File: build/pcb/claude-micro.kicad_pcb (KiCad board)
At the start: 2 copper layers, 128 x 88 mm, 95 parts, among them SW1 Kailh Choc v1, SW10 Kailh Choc v1, SW11 Kailh Choc v1, SW12 Kailh Choc v1, SW13 Kailh Choc v1, SW2 Kailh Choc v1, SW3 Kailh Choc v1, SW4 Kailh Choc v1, SW5 Kailh Choc v1, SW6 Kailh Choc v1, SW7 Kailh Choc v1, SW8 Kailh Choc v1, SW9 Kailh Choc v1, U2 74LVC1G17

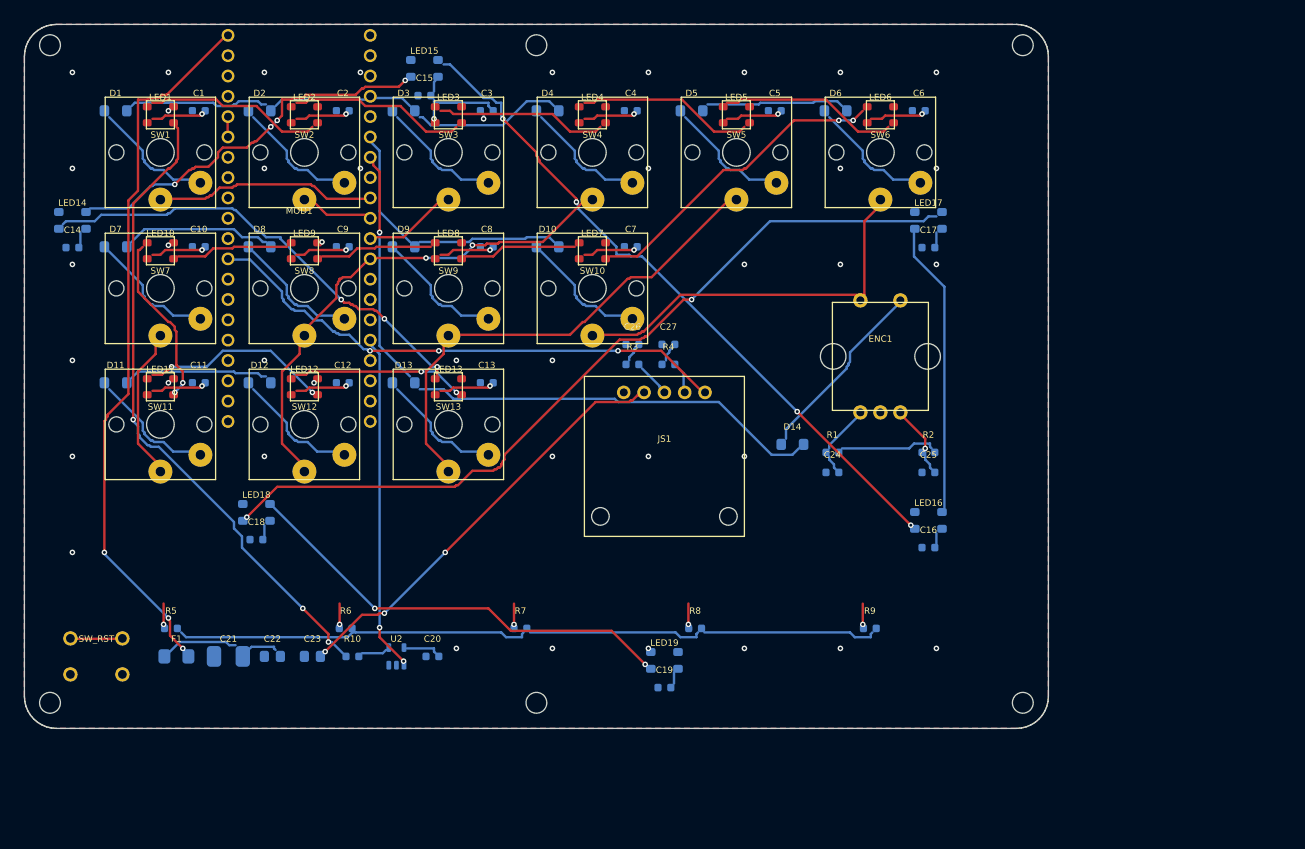
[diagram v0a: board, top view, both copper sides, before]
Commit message: Switch to clear MX switches; fix the EasyEDA project wrapper
Two changes.

EasyEDA
-------
The project wrapper now matches what EasyEDA 6.5 actually writes: docType is
the string "5" (not the integer 5), colors is an object, editorVersion sits at
the top level alongside a description, and each sheet carries its own string
docType and description. The 4.x shape I had reverse-engineered from an older
exported file would not round-trip. The structural test now asserts the exact
key set and types on both the project and the sheet.

Switches
--------
Kailh Choc low-profile replaced with clear-housing MX-compatible switches,
5-pin PCB mount. That is not a drop-in: MX needs a 19.05 mm grid where Choc
ran at 18 x 17, so the whole device re-derives from the config.

- footprint: two contacts at (-3.81, 2.54) and (2.54, 5.08), centre boss and
  two locating posts, 14 mm plate cutout, both contacts on the south half so
  the north half stays clear for the per-key LED in the switch's light window
- keycaps: 18 x 18 mm with a cross socket instead of Choc's twin posts, so
  bought MX caps drop in as an alternative to printing them
- Z stack rebuilt for 4 mm travel and an 11.6 mm body; the taller stack means
  the encoder now takes a stock 12.5 mm shaft rather than a trimmed one
- board 128 x 88 -> 159 x 102 mm, case 134 x 94 -> 165 x 108 mm, and the MCU
  module moved to the gutters of the new grid (pin columns at x=9.25 and
  x=27.03) so its through-holes still miss every top-side pad
- switches render translucent in the viewer to match the clear housings

The switch footprint name is now read from the config rather than hardcoded in
the ERC and two tests, which is what caught the 0-switches-for-13-keys error
after the swap.

Rebuilt and re-verified: 141/141 connections routed, 0 DRC errors, 0 warnings,
9/9 meshes watertight, 36/36 checks passing.

Co-Authored-By: Claude Opus 5 <noreply@anthropic.com>
Claude-Session: https://claude.ai/code/session_018r1gdNJN1A3uPDEU4991Ag
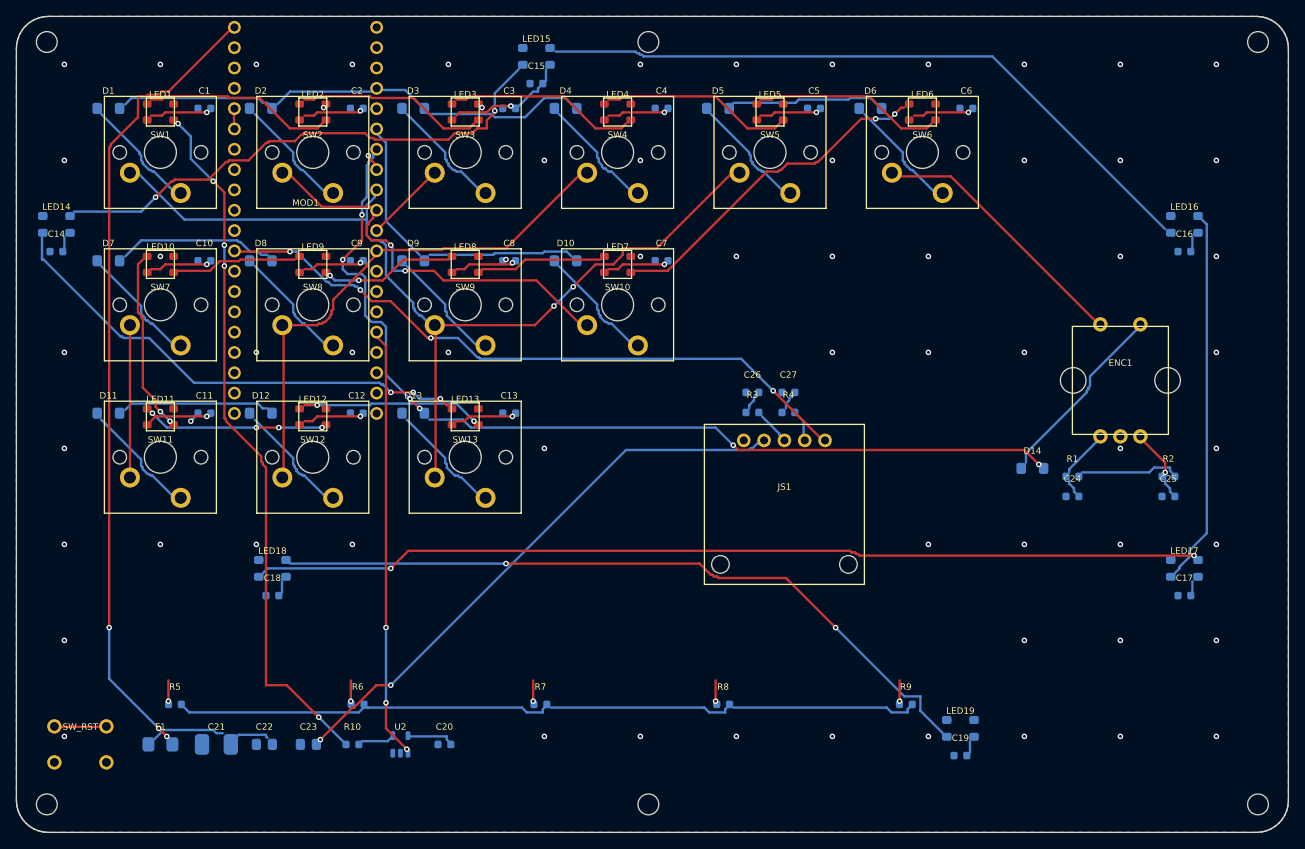
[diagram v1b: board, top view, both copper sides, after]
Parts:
- removed the ? at (-13.8, -13.4)
- removed the ? at (47.0, -13.4)
- removed the ? at (107.8, -13.4)
- removed the ? at (-13.8, 68.8)
- removed the ? at (47.0, 68.8)
- removed the ? at (107.8, 68.8)
- added ?: , claude-micro:MountingHole, F.Cu at (-14.2, -13.8)
- added ?: , claude-micro:MountingHole, F.Cu at (61.0, -13.8)
- added ?: , claude-micro:MountingHole, F.Cu at (137.2, -13.8)
- added ?: , claude-micro:MountingHole, F.Cu at (-14.2, 81.5)
- added ?: , claude-micro:MountingHole, F.Cu at (61.0, 81.5)
- added ?: , claude-micro:MountingHole, F.Cu at (137.2, 81.5)
- SW1, SW10, SW11, SW12, SW13, SW2, SW3, SW4, SW5, SW6, SW7, SW8, SW9: value Kailh Choc v1 -> MX clear; footprint claude-micro:Choc_v1 -> claude-micro:MX_PCB
- moved C17 54.0 mm to (128.0, 55.4)
- moved LED17 54.0 mm to (128.0, 52.0)
- moved C16 48.9 mm to (128.0, 12.4)
- moved LED16 48.9 mm to (128.0, 9.00)
- moved C19 38.0 mm to (100.0, 75.4)
- moved LED19 38.0 mm to (100.0, 72.0)
- moved C24 30.1 mm to (114.0, 43.0)
- moved C25 30.1 mm to (126.0, 43.0)
- moved D14 30.1 mm to (109.0, 39.5)
- moved ENC1 30.1 mm to (120.0, 28.5)
- moved R1 30.1 mm to (114.0, 40.5)
- moved R2 30.1 mm to (126.0, 40.5)
- moved C26 16.2 mm to (74.0, 30.0)
- moved C27 16.2 mm to (78.5, 30.0)
- moved JS1 16.2 mm to (78.0, 44.0)
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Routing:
- net ROW3: track 79.8 -> 117.6 mm, vias 1 -> 6
- net LED_D18: track 54.5 -> 91.4 mm
- net COL0: track 81.9 -> 111.3 mm, vias 0 -> 2
- net COL1: track 52.6 -> 78.8 mm, vias 0 -> 2
- net LED_D14: track 47.6 -> 65.6 mm, vias 4 -> 2
- net +3V3: track 65.6 -> 83.3 mm, vias 3 -> 2
- net JOY_SW: track 65.5 -> 82.0 mm, vias 3 -> 4
- net LED_D17: track 102.4 -> 117.8 mm
- net +5V: track 112.7 -> 127.0 mm
- net LED_DIN_3V3: track 41.1 -> 52.9 mm, vias 2 -> 3
- net VBUS: track 88.1 -> 99.3 mm
- net LED_D16: track 36.0 -> 46.1 mm
- net LED_DIN: track 80.1 -> 87.3 mm, vias 3 -> 5
- net ROW2: track 49.1 -> 53.7 mm
- net TOUCH_DRV: track 87.5 -> 91.7 mm
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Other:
- board size 128 x 88 mm -> 159 x 102 mm
